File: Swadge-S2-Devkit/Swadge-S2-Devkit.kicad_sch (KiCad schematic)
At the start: 91 parts, among them J1 CurrentMonitor, J2 DEBUG_BANK_C, J3 DEBUG_BANK_B, J4 DEBUG_BANK_A, J5 MICSEL, J6 TRYMIC, J7 LEDK_J, J8 LCD18, J9 LCD28, M1 VZ43FC1B5640007L, P1 USB_C_Plug_USB2.0, Q1 Q_N_FET, Q2 AP2003_PN_FET, Q3 AP2003_PN_FET, Q4 AP2003_PN_FET, SW1 4-1437565-2, SW10 BLISTER_SILICONE_BUTTON, SW11 touch-ring-6, SW14 SW_SPDT, SW2 4-1437565-2, SW3 4-1437565-2, SW4 4-1437565-2, SW5 4-1437565-2, SW6 4-1437565-2, SW7 4-1437565-2, SW8 4-1437565-2, SW9 4-1437565-2, U1 ESP32-S2-SOLO, U10 GENERIC_LDO_2.8, U11 LCD_240x240_1.3_12, U12 LCD_135x240_1.14_13, U15 LCD_240x240_1.54_12, U2 BUS_PCIexpress, U3 MT3410, U4 GS321-TR, U6 INGHAi_GSPK2308P-8R0.5W, U9 GENERIC_LDO_1.8

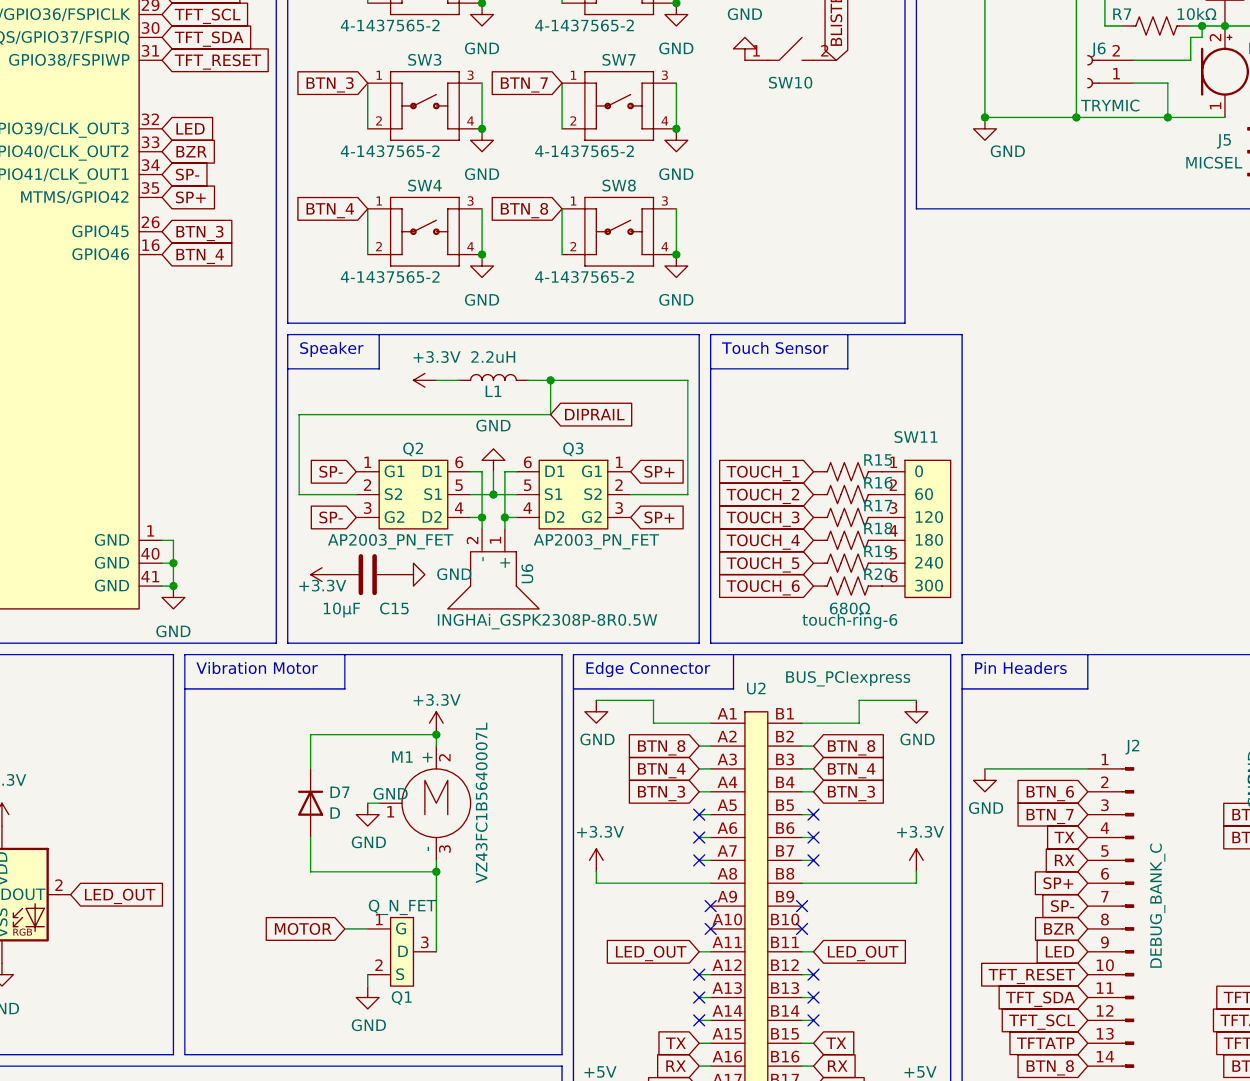
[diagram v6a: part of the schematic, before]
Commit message: Removed speaker
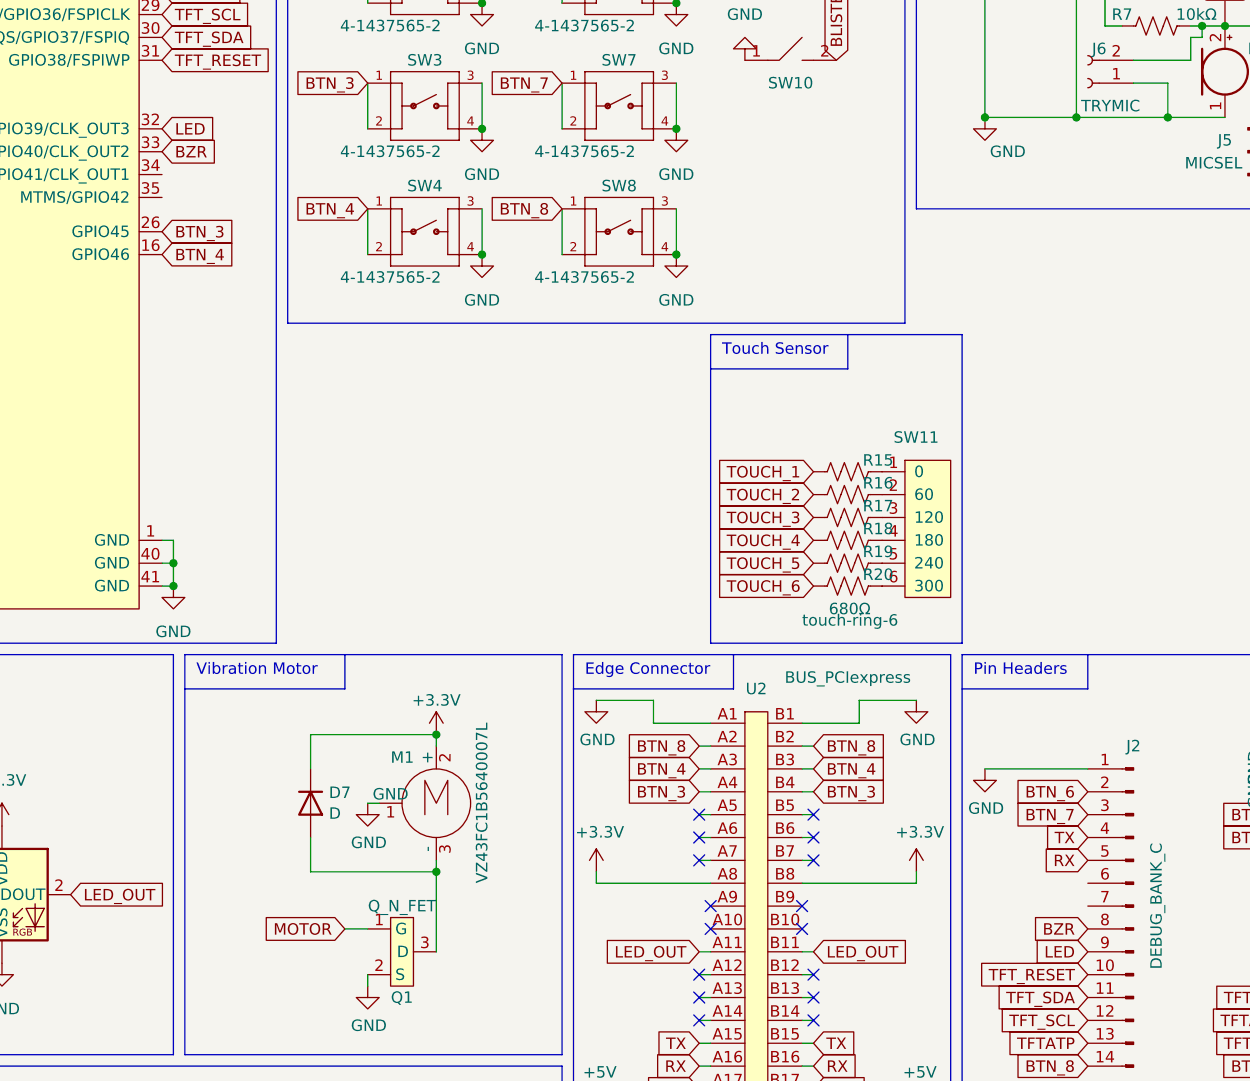
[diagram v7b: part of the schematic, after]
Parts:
- removed C15: 10μF, Swadge_Parts:C_0603_1608Metric, symbol Swadge_Parts:C
- removed L1: 2.2uH, Swadge_Parts:L_1008_2520Metric, symbol Swadge_Parts:L
- removed Q2, Q3: AP2003_PN_FET, Swadge_Parts:SOT-23-6, symbol Swadge_Parts:AP2003_PN_FET
- removed U6: INGHAi_GSPK2308P-8R0.5W, Swadge_Parts:INGHAi GSPK2308P-8R0.5W, symbol Swadge_Parts:INGHAi_GSPK2308P-8R0.5W
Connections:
- net SP+: no longer names the net of U1.35 (MTMS/GPIO42)
- net SP+: no longer J2.6 (Pin_6)
- net SP-: no longer names the net of U1.34 (MTDI/GPIO41/CLK_OUT1)
- net SP-: no longer J2.7 (Pin_7)
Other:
- note removed: "Speaker"

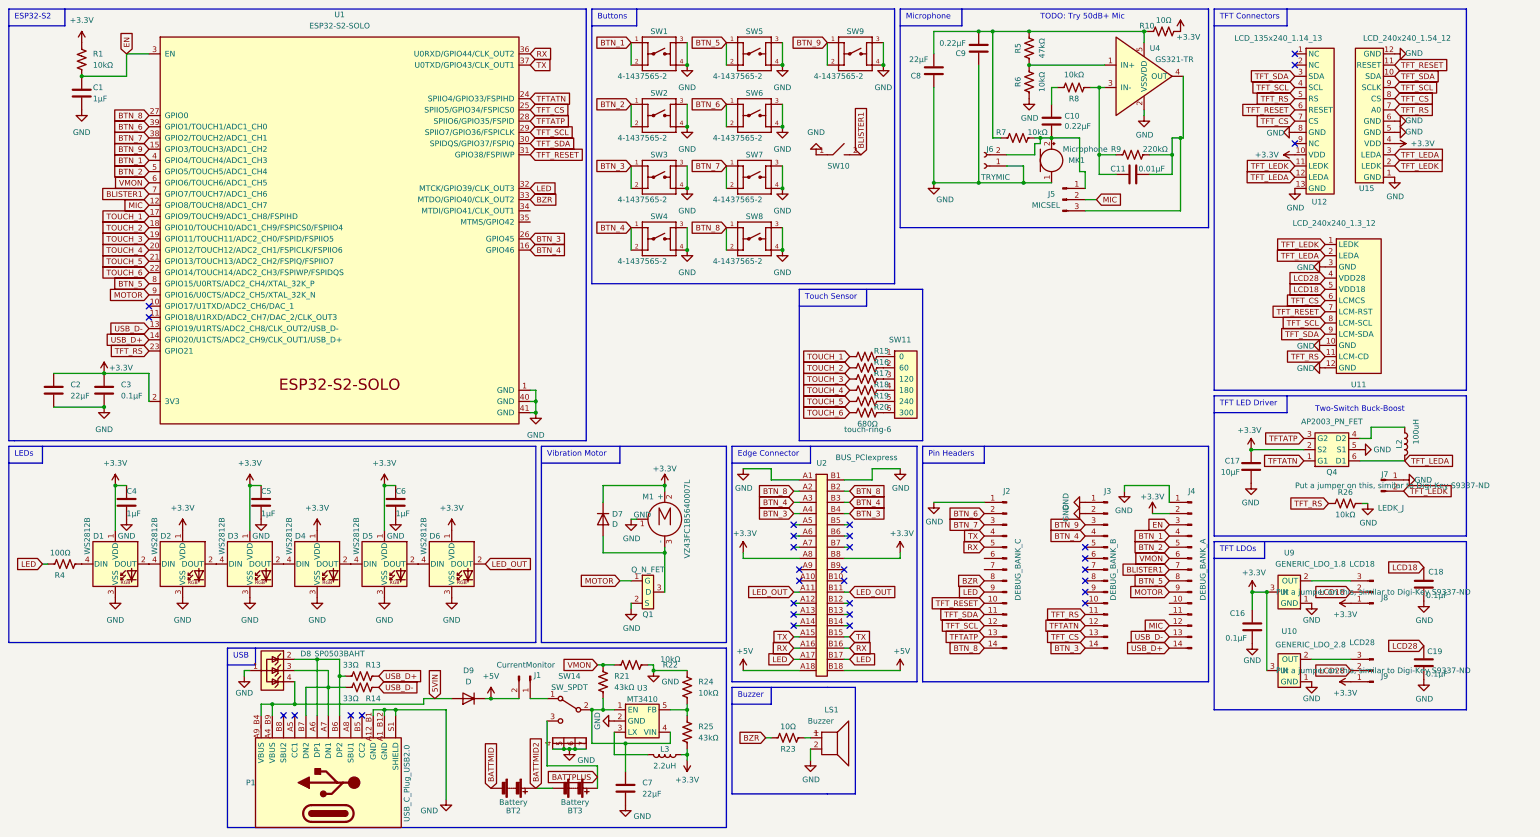
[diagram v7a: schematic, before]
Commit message: Removed vibration motor
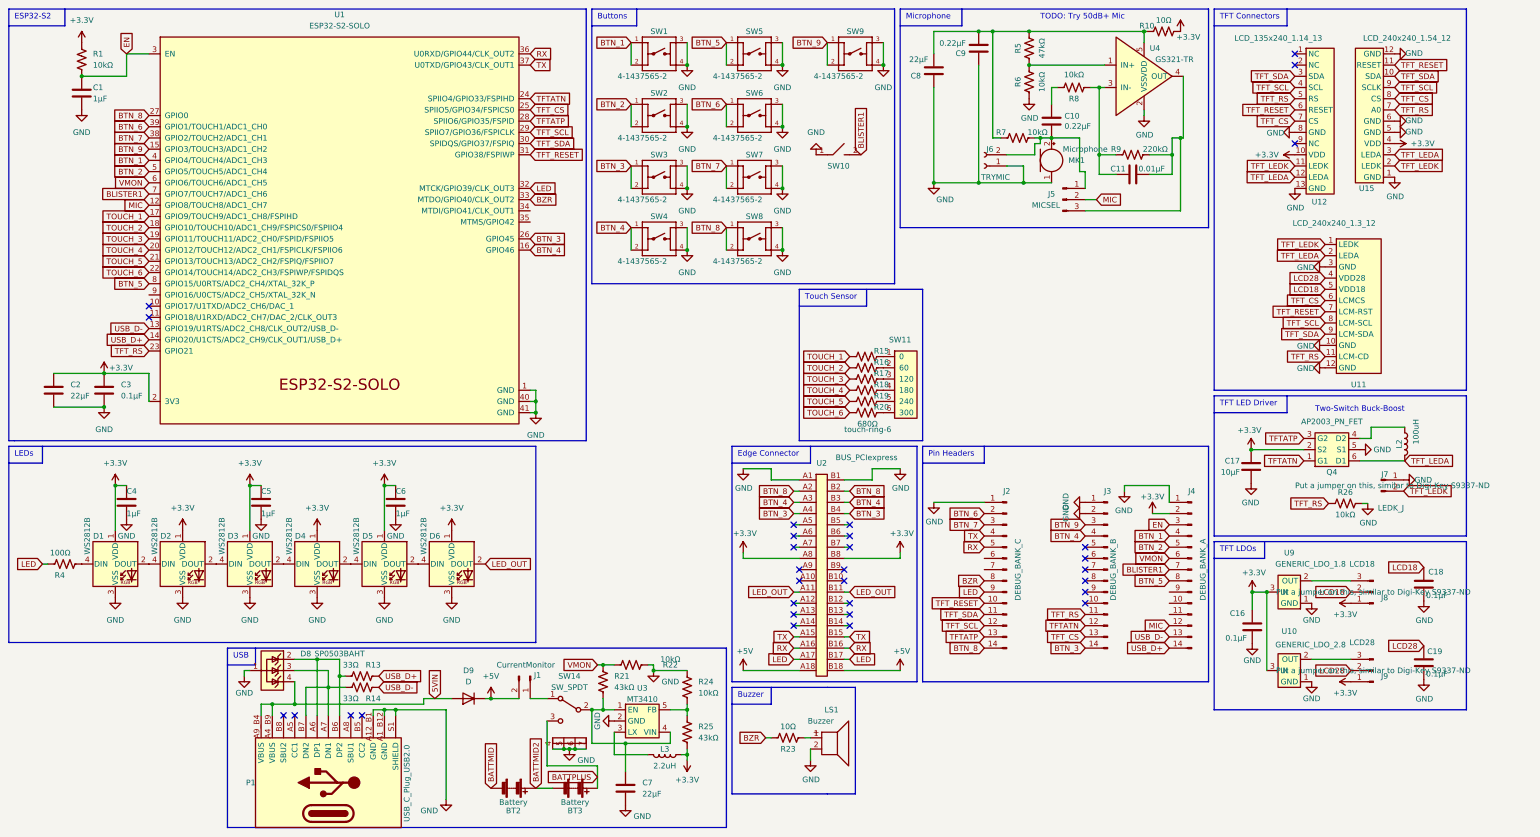
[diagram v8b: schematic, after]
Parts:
- removed D7: D, Swadge_Parts:D_SMA, symbol Swadge_Parts:D
- removed M1: VZ43FC1B5640007L, Swadge_Parts:VZ43FC1B5640007L, symbol Swadge_Parts:VZ43FC1B5640007L
- removed Q1: Q_N_FET, Swadge_Parts:SOT-23, symbol Swadge_Parts:Q_N_FET
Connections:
- net MOTOR: no longer names the net of U1.9 (GPIO16/U0CTS/ADC2_CH5/XTAL_32K_N)
- net MOTOR: no longer J4.9 (Pin_9)
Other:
- note removed: "Vibration Motor"
